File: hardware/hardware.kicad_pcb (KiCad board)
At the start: 2 copper layers, 1 part

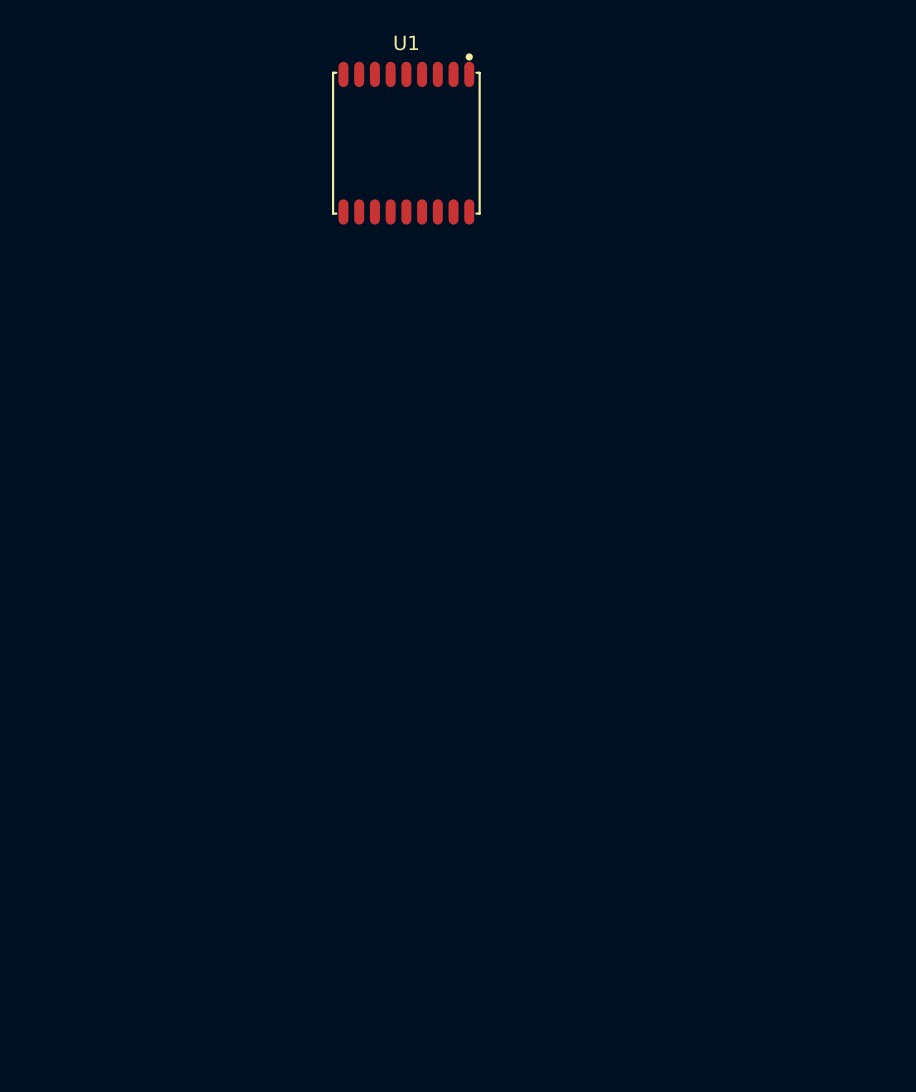
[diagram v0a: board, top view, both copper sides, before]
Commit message: place all components on pcb
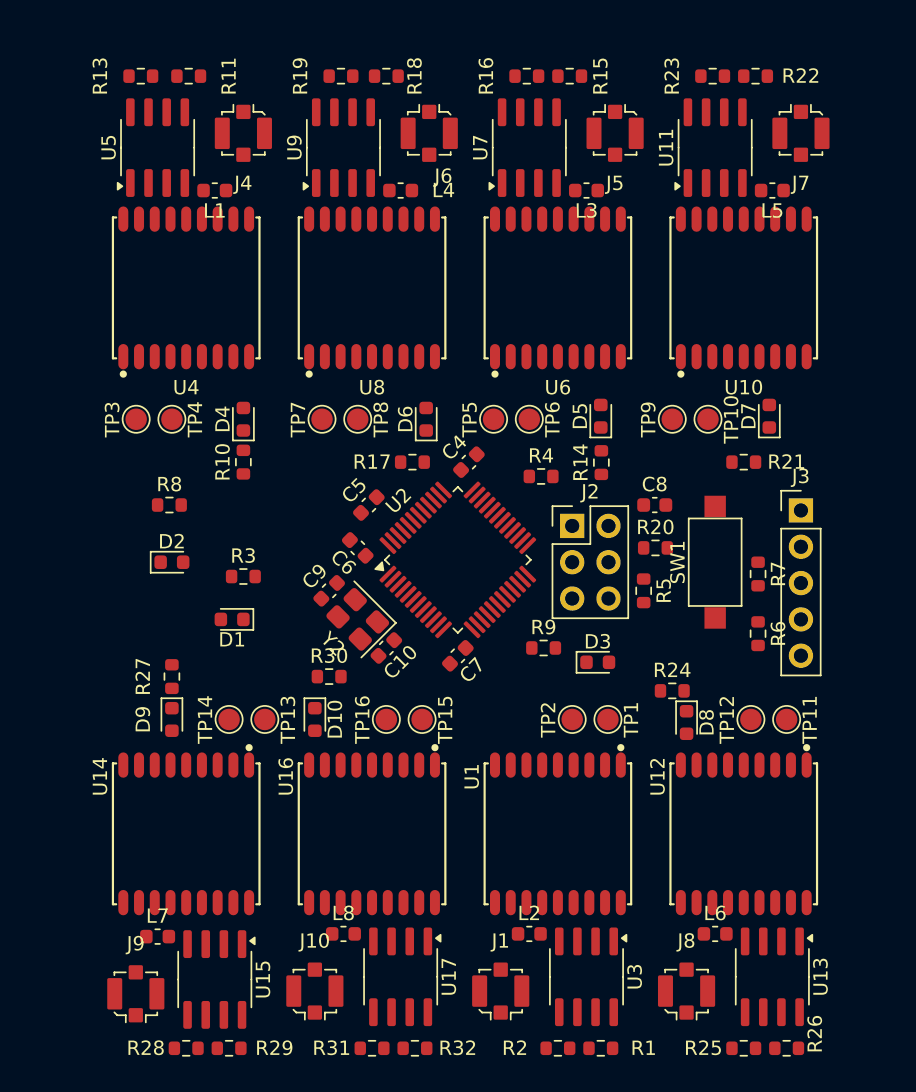
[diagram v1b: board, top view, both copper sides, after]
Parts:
- added C10: 20p, Capacitor_SMD:C_0603_1608Metric, F.Cu at (100.0, 107.0)
- added C4: 100n, Capacitor_SMD:C_0603_1608Metric, F.Cu at (105.8, 94.0)
- added C5: 100n, Capacitor_SMD:C_0603_1608Metric, F.Cu at (98.8, 97.0)
- added C6: 100n, Capacitor_SMD:C_0603_1608Metric, F.Cu at (98.0, 100.0)
- added C7: 100n, Capacitor_SMD:C_0603_1608Metric, F.Cu at (105.0, 107.5)
- added C8: 1u, Capacitor_SMD:C_0603_1608Metric, F.Cu at (118.8, 97.0)
- added C9: 20p, Capacitor_SMD:C_0603_1608Metric, F.Cu at (96.0, 103.0)
- added D1: LED, LED_SMD:LED_0603_1608Metric, F.Cu at (89.2, 105.0)
- added D10: LED, LED_SMD:LED_0603_1608Metric, F.Cu at (95.0, 112.0)
- added D2: LED, Diode_SMD:D_0603_1608Metric, F.Cu at (85.0, 101.0)
- added D3: LED, Diode_SMD:D_0603_1608Metric, F.Cu at (114.8, 108.0)
- added D4: LED, LED_SMD:LED_0603_1608Metric, F.Cu at (90.0, 91.0)
- added D5: LED, LED_SMD:LED_0603_1608Metric, F.Cu at (115.0, 90.8)
- added D6: LED, LED_SMD:LED_0603_1608Metric, F.Cu at (102.8, 91.0)
- added D7: LED, LED_SMD:LED_0603_1608Metric, F.Cu at (126.8, 90.8)
- added D8: LED, LED_SMD:LED_0603_1608Metric, F.Cu at (121.0, 112.2)
- added D9: LED, LED_SMD:LED_0603_1608Metric, F.Cu at (85.0, 112.0)
- added J1: Conn_Coaxial, Connector_Coaxial:U.FL_Molex_MCRF_73412-0110_Vertical, F.Cu at (108.0, 131.0)
- added J10: Conn_Coaxial, Connector_Coaxial:U.FL_Molex_MCRF_73412-0110_Vertical, F.Cu at (95.0, 131.0)
- added J2: BOOT, Connector_PinHeader_2.54mm:PinHeader_2x03_P2.54mm_Vertical, F.Cu at (113.0, 98.5)
- added J3: SWD, Connector_PinHeader_2.54mm:PinHeader_1x05_P2.54mm_Vertical, F.Cu at (129.0, 97.4)
- added J4: Conn_Coaxial, Connector_Coaxial:U.FL_Molex_MCRF_73412-0110_Vertical, F.Cu at (90.0, 71.0)
- added J5: Conn_Coaxial, Connector_Coaxial:U.FL_Molex_MCRF_73412-0110_Vertical, F.Cu at (116.0, 71.0)
- added J6: Conn_Coaxial, Connector_Coaxial:U.FL_Molex_MCRF_73412-0110_Vertical, F.Cu at (103.0, 71.0)
- added J7: Conn_Coaxial, Connector_Coaxial:U.FL_Molex_MCRF_73412-0110_Vertical, F.Cu at (129.0, 71.0)
- added J8: Conn_Coaxial, Connector_Coaxial:U.FL_Molex_MCRF_73412-0110_Vertical, F.Cu at (121.0, 131.0)
- added J9: Conn_Coaxial, Connector_Coaxial:U.FL_Molex_MCRF_73412-0110_Vertical, F.Cu at (82.5, 131.2)
- added L1: L_Small, Inductor_SMD:L_0603_1608Metric, F.Cu at (88.0, 75.0)
- added L2: L_Small, Inductor_SMD:L_0603_1608Metric, F.Cu at (110.0, 127.0)
- added L3: L_Small, Inductor_SMD:L_0603_1608Metric, F.Cu at (114.0, 75.0)
- added L4: L_Small, Inductor_SMD:L_0603_1608Metric, F.Cu at (101.0, 75.0)
- added L5: L_Small, Inductor_SMD:L_0603_1608Metric, F.Cu at (127.0, 75.0)
- added L6: L_Small, Inductor_SMD:L_0603_1608Metric, F.Cu at (123.0, 127.0)
- added L7: L_Small, Inductor_SMD:L_0603_1608Metric, F.Cu at (84.0, 127.2)
- added L8: L_Small, Inductor_SMD:L_0603_1608Metric, F.Cu at (97.0, 127.0)
- added R1: R_Small, Resistor_SMD:R_0603_1608Metric, F.Cu at (115.0, 135.0)
- added R10: 5K, Resistor_SMD:R_0603_1608Metric, F.Cu at (90.0, 94.0)
- added R11: R_Small, Resistor_SMD:R_0603_1608Metric, F.Cu at (86.2, 67.0)
- added R13: R_Small, Resistor_SMD:R_0603_1608Metric, F.Cu at (82.8, 67.0)
- added R14: 5K, Resistor_SMD:R_0603_1608Metric, F.Cu at (115.0, 94.0)
- added R15: R_Small, Resistor_SMD:R_0603_1608Metric, F.Cu at (112.8, 67.0)
- added R16: R_Small, Resistor_SMD:R_0603_1608Metric, F.Cu at (109.8, 67.0)
- added R17: 5K, Resistor_SMD:R_0603_1608Metric, F.Cu at (101.8, 94.0)
- added R18: R_Small, Resistor_SMD:R_0603_1608Metric, F.Cu at (100.0, 67.0)
- added R19: R_Small, Resistor_SMD:R_0603_1608Metric, F.Cu at (96.8, 67.0)
- added R2: R_Small, Resistor_SMD:R_0603_1608Metric, F.Cu at (112.0, 135.0)
- added R20: 10k, Resistor_SMD:R_0603_1608Metric, F.Cu at (118.8, 100.0)
- added R21: 5K, Resistor_SMD:R_0603_1608Metric, F.Cu at (125.0, 94.0)
- added R22: R_Small, Resistor_SMD:R_0603_1608Metric, F.Cu at (125.8, 67.0)
- added R23: R_Small, Resistor_SMD:R_0603_1608Metric, F.Cu at (122.8, 67.0)
- added R24: 5K, Resistor_SMD:R_0603_1608Metric, F.Cu at (120.0, 110.0)
- added R25: R_Small, Resistor_SMD:R_0603_1608Metric, F.Cu at (125.0, 135.0)
- added R26: R_Small, Resistor_SMD:R_0603_1608Metric, F.Cu at (128.0, 135.0)
- added R27: 5K, Resistor_SMD:R_0603_1608Metric, F.Cu at (85.0, 109.0)
- added R28: R_Small, Resistor_SMD:R_0603_1608Metric, F.Cu at (86.0, 135.0)
- added R29: R_Small, Resistor_SMD:R_0603_1608Metric, F.Cu at (89.0, 135.0)
- added R3: 5K, Resistor_SMD:R_0603_1608Metric, F.Cu at (90.0, 102.0)
- added R30: 5K, Resistor_SMD:R_0603_1608Metric, F.Cu at (96.0, 109.0)
- added R31: R_Small, Resistor_SMD:R_0603_1608Metric, F.Cu at (99.0, 135.0)
- added R32: R_Small, Resistor_SMD:R_0603_1608Metric, F.Cu at (102.0, 135.0)
- added R4: 100k, Resistor_SMD:R_0603_1608Metric, F.Cu at (110.8, 95.0)
- added R5: 100k, Resistor_SMD:R_0603_1608Metric, F.Cu at (118.0, 103.0)
- added R6: 10k, Resistor_SMD:R_0603_1608Metric, F.Cu at (126.0, 106.0)
- added R7: 10k, Resistor_SMD:R_0603_1608Metric, F.Cu at (126.0, 101.8)
- added R8: 10k, Resistor_SMD:R_0603_1608Metric, F.Cu at (84.8, 97.0)
- added R9: 10k, Resistor_SMD:R_0603_1608Metric, F.Cu at (111.0, 107.0)
- added SW1: SW_Push, Button_Switch_SMD:SW_SPST_CK_RS282G05A3, F.Cu at (123.0, 101.0)
- added TP1: TestPoint, TestPoint:TestPoint_Pad_D1.5mm, F.Cu at (115.5, 112.0)
- added TP10: TestPoint, TestPoint:TestPoint_Pad_D1.5mm, F.Cu at (122.5, 91.0)
- added TP11: TestPoint, TestPoint:TestPoint_Pad_D1.5mm, F.Cu at (128.0, 112.0)
- added TP12: TestPoint, TestPoint:TestPoint_Pad_D1.5mm, F.Cu at (125.5, 112.0)
- added TP13: TestPoint, TestPoint:TestPoint_Pad_D1.5mm, F.Cu at (91.5, 112.0)
- added TP14: TestPoint, TestPoint:TestPoint_Pad_D1.5mm, F.Cu at (89.0, 112.0)
- added TP15: TestPoint, TestPoint:TestPoint_Pad_D1.5mm, F.Cu at (102.5, 112.0)
- added TP16: TestPoint, TestPoint:TestPoint_Pad_D1.5mm, F.Cu at (100.0, 112.0)
- added TP2: TestPoint, TestPoint:TestPoint_Pad_D1.5mm, F.Cu at (113.0, 112.0)
- added TP3: TestPoint, TestPoint:TestPoint_Pad_D1.5mm, F.Cu at (82.5, 91.0)
- added TP4: TestPoint, TestPoint:TestPoint_Pad_D1.5mm, F.Cu at (85.0, 91.0)
- added TP5: TestPoint, TestPoint:TestPoint_Pad_D1.5mm, F.Cu at (107.5, 91.0)
- added TP6: TestPoint, TestPoint:TestPoint_Pad_D1.5mm, F.Cu at (110.0, 91.0)
- added TP7: TestPoint, TestPoint:TestPoint_Pad_D1.5mm, F.Cu at (95.5, 91.0)
- added TP8: TestPoint, TestPoint:TestPoint_Pad_D1.5mm, F.Cu at (98.0, 91.0)
- added TP9: TestPoint, TestPoint:TestPoint_Pad_D1.5mm, F.Cu at (120.0, 91.0)
- added U10: ~, ATGM336H:GPSM-SMD_ATGM336H-TR, F.Cu at (125.0, 81.8)
- added U11: 24LC32, Package_SO:SOIC-8_3.9x4.9mm_P1.27mm, F.Cu at (123.0, 72.0)
- added U12: ~, ATGM336H:GPSM-SMD_ATGM336H-TR, F.Cu at (125.0, 120.0)
- added U13: 24LC32, Package_SO:SOIC-8_3.9x4.9mm_P1.27mm, F.Cu at (127.0, 130.0)
- added U14: ~, ATGM336H:GPSM-SMD_ATGM336H-TR, F.Cu at (86.0, 120.0)
- added U15: 24LC32, Package_SO:SOIC-8_3.9x4.9mm_P1.27mm, F.Cu at (88.0, 130.2)
- added U16: ~, ATGM336H:GPSM-SMD_ATGM336H-TR, F.Cu at (99.0, 120.0)
- added U17: 24LC32, Package_SO:SOIC-8_3.9x4.9mm_P1.27mm, F.Cu at (101.0, 130.0)
- added U2: STM32F103C8Tx, Package_QFP:LQFP-48_7x7mm_P0.5mm, F.Cu at (105.0, 100.8)
- added U3: 24LC32, Package_SO:SOIC-8_3.9x4.9mm_P1.27mm, F.Cu at (114.0, 130.0)
- added U4: ~, ATGM336H:GPSM-SMD_ATGM336H-TR, F.Cu at (86.0, 81.8)
- added U5: 24LC32, Package_SO:SOIC-8_3.9x4.9mm_P1.27mm, F.Cu at (84.0, 72.0)
- added U6: ~, ATGM336H:GPSM-SMD_ATGM336H-TR, F.Cu at (112.0, 81.8)
- added U7: 24LC32, Package_SO:SOIC-8_3.9x4.9mm_P1.27mm, F.Cu at (110.0, 72.0)
- added U8: ~, ATGM336H:GPSM-SMD_ATGM336H-TR, F.Cu at (99.0, 81.8)
- added U9: 24LC32, Package_SO:SOIC-8_3.9x4.9mm_P1.27mm, F.Cu at (97.0, 72.0)
- added Y2: Crystal_GND24, Crystal:Crystal_SMD_3225-4Pin_3.2x2.5mm, F.Cu at (98.0, 105.0)
- moved U1 49.5 mm to (112.0, 120.0)
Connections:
- U1 pad 10: unconnected-(U1-GND-Pad10) -> GND
- U1 pad 11: unconnected-(U1-RF_IN-Pad11) -> Net-(J1-In)
- U1 pad 12: unconnected-(U1-GND-Pad12) -> GND
- U1 pad 14: unconnected-(U1-VCC_RF-Pad14) -> Net-(U1-VCC_RF)
- U1 pad 16: unconnected-(U1-SDA-Pad16) -> Net-(U1-SDA)
- U1 pad 17: unconnected-(U1-SCL-Pad17) -> Net-(U1-SCL)
- U1 pad 2: unconnected-(U1-TXD-Pad2) -> RX_1
- U1 pad 3: unconnected-(U1-RXD-Pad3) -> TX_1
- U1 pad 4: unconnected-(U1-1PPS-Pad4) -> Net-(D1-A)
- U1 pad 8: unconnected-(U1-VCC-Pad8) -> +3.3V
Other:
- copper layers 2 -> 4

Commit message: add power and comm connector
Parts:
- added J11: Conn_01x06_Pin, Connector_JST:JST_SH_BM06B-SRSS-TB_1x06-1MP_P1.00mm_Vertical, F.Cu at (82.0, 100.5)
- moved D2 9.69 mm to (94.2, 98.0)
- moved R8 5.44 mm to (90.2, 98.0)

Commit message: full wiring pcb
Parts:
- removed R4, R5: 100k, Resistor_SMD:R_0603_1608Metric
- moved D3 37.3 mm to (77.5, 107.5)
- moved R9 30.5 mm to (80.5, 107.5), turned to 180 degrees
- moved D1 22.0 mm to (110.0, 112.2), turned to -90 degrees
- moved R3 21.2 mm to (110.0, 109.2), turned to -90 degrees
- moved D2 17.1 mm to (77.3, 95.5)
- moved R8 10.2 mm to (80.3, 95.5), turned to 180 degrees
- moved J11 4.12 mm to (78.0, 101.5)
- moved D4 1.54 mm to (91.0, 89.8)
- moved R10 1.54 mm to (91.0, 92.8)
- moved TP3 1.50 mm to (84.0, 91.0)
- moved TP4 1.50 mm to (86.5, 91.0)
- moved R20 1.45 mm to (120.1, 100.7), turned to 90 degrees
- moved C8 1.45 mm to (120.1, 97.6), turned to 90 degrees
- moved D8 1.02 mm to (120.0, 112.0)
- moved D6 1.00 mm to (102.8, 90.0)
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- renumbered SW1 to RST
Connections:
- J2 pad 3: Net-(J2-Pin_3) -> BOOT0
- J2 pad 4: Net-(J2-Pin_4) -> BOOT1
- U2 pad 29: unconnected-(U2-PA8-Pad29) -> LED2
- U2 pad 30: unconnected-(U2-PA9-Pad30) -> LED1
- U2 pad 7: RST -> RESET
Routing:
- net GND: track 0.00 -> 236.4 mm, vias 0 -> 78
- net +3.3V: track 0.00 -> 106.1 mm, vias 0 -> 39
- net RESET: track 0.00 -> 41.6 mm, vias 0 -> 2
- net SWCLK: track 0.00 -> 41.1 mm, vias 0 -> 1
- net LED2: track 0.00 -> 37.9 mm, vias 0 -> 2
- net RX_2: track 0.00 -> 37.7 mm
- net TX_2: track 0.00 -> 34.6 mm
- net SWDIO: track 0.00 -> 32.8 mm, vias 0 -> 1
- net LED1: track 0.00 -> 31.7 mm, vias 0 -> 2
- net RX_6: track 0.00 -> 31.1 mm, vias 0 -> 2
- net SS: track 0.00 -> 29.5 mm, vias 0 -> 2
- net MOSI: track 0.00 -> 29.2 mm, vias 0 -> 2
- net MISO: track 0.00 -> 28.8 mm, vias 0 -> 2
- net TX_7: track 0.00 -> 27.9 mm
- net TX_6: track 0.00 -> 27.8 mm
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- added copper zone on F.Cu, net +3.3V
- added copper zone on In2.Cu, net +3.3V
- added copper zone on F.Cu, net GND
- added copper zone on In1.Cu, net GND
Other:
- board outline added: 60 x 71 mm

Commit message: add connector step
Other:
- outline, holes or cut-outs redrawn
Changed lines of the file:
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@@
 		)
 		(embedded_fonts no)
-		(model "${KICAD9_3DMODEL_DIR}/Connector_JST.3dshapes/JST_SH_BM06B-SRSS-TB_1x06-1MP_P1.00mm_Vertical.step"
+		(model "/Users/ronanmingon/Downloads/jst-sh-smd-connectors-1.snapshot.4/SMxxB-SRSS-TB/SM06B-SRSS-TB.STEP"
 			(offset
-				(xyz 0 0 0)
+				(xyz 0 -1 -0.4)
 			)
 			(scale
@@
 			)
 			(rotate
-				(xyz 0 0 0)
+				(xyz -90 -0 -180)
 			)
 		)
@@
 		)
 	)
+	(gr_circle
+		(center 132 91)
+		(end 133.6 91)
+		(stroke
+			(width 0.1)
+			(type solid)
+		)
+		(fill no)
+		(layer "Edge.Cuts")
+	)
 	(gr_line
 		(start 132 65)
@@
 		(layer "Edge.Cuts")
 	)
+	(gr_circle
+		(center 132 112)
+		(end 133.6 112)
+		(stroke
+			(width 0.1)
+			(type solid)
+		)
+		(fill no)
+		(layer "Edge.Cuts")
+	)
+	(gr_circle
+		(center 78 91)
+		(end 79.6 91)
+		(stroke
+			(width 0.1)
+			(type solid)
+		)
+		(fill no)
+		(layer "Edge.Cuts")
+	)
+	(gr_circle
+		(center 78 112)
+		(end 79.6 112)
+		(stroke
+			(width 0.1)
+			(type solid)
+		)
+		(fill no)
+		(layer "Edge.Cuts")
+	)

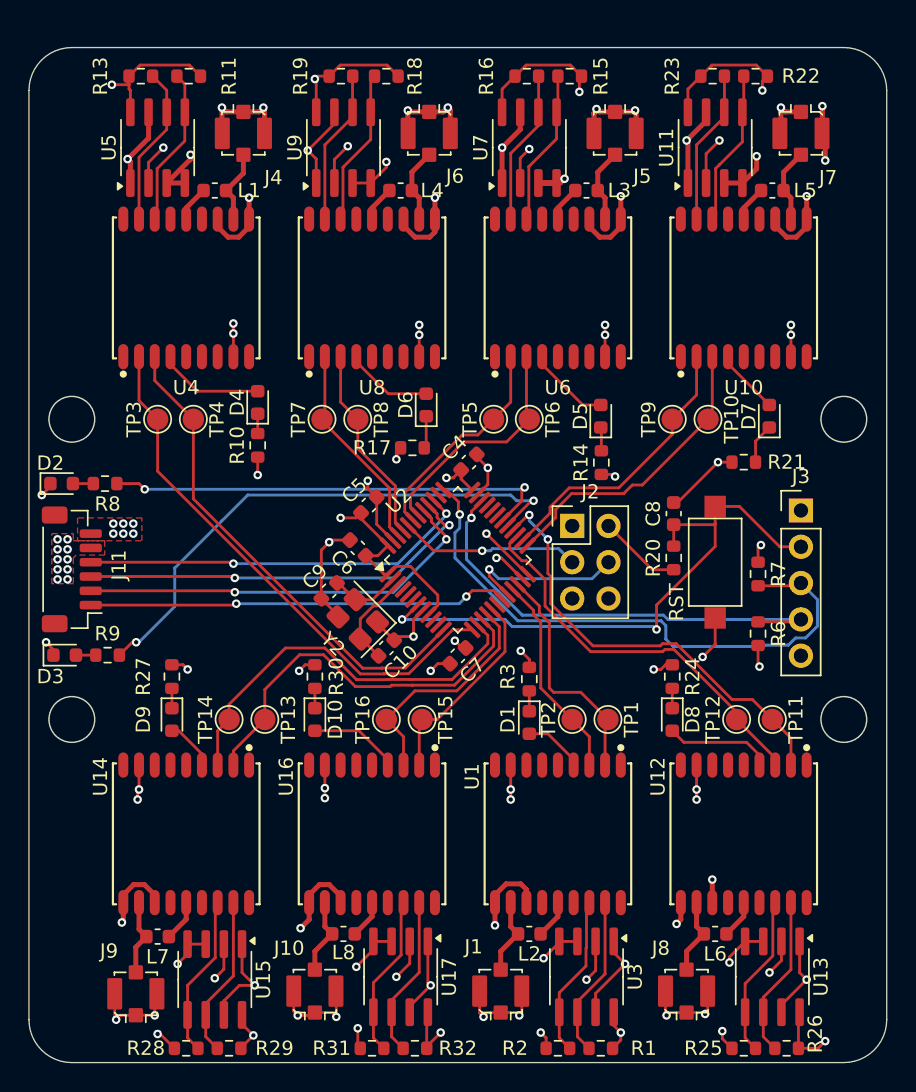
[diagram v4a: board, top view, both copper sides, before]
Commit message: fix gnss ground module
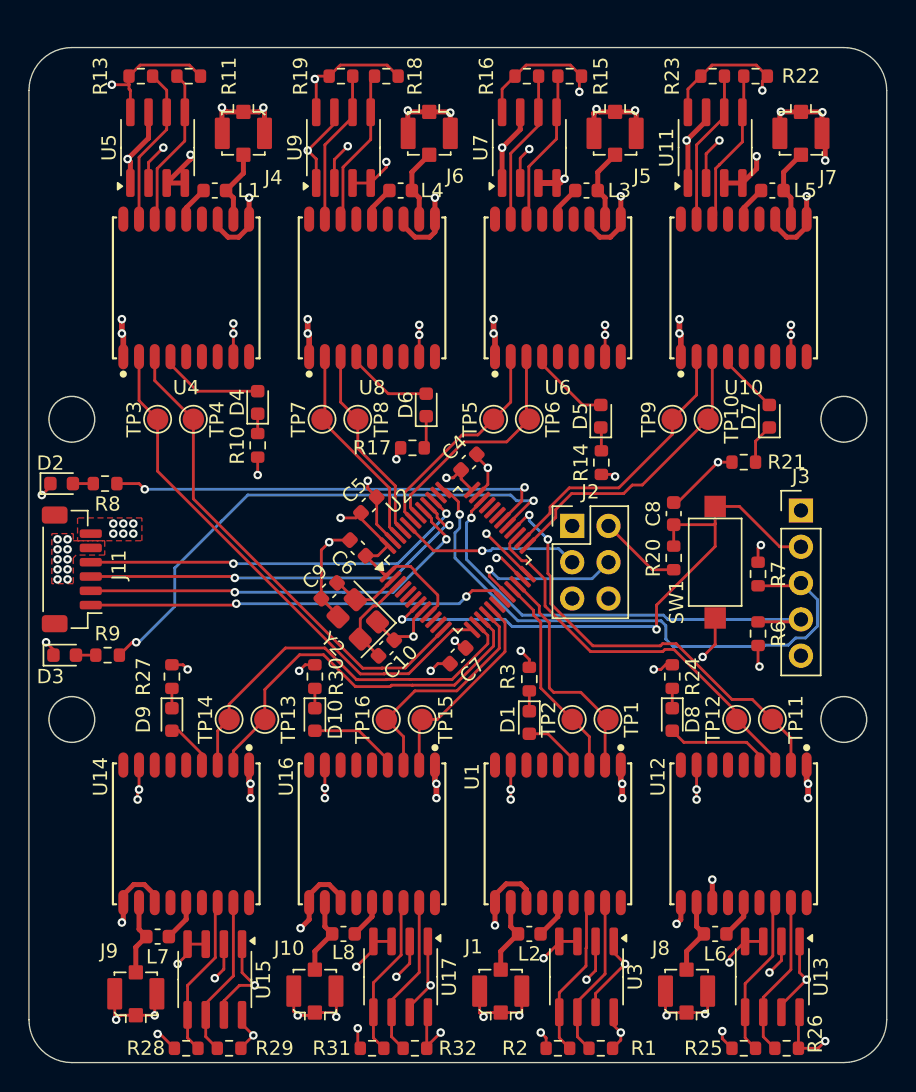
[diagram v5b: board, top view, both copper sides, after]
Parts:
- renumbered RST to SW1
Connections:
- U1 pad 1: unconnected-(U1-GND-Pad1) -> GND
- U10 pad 1: unconnected-(U10-GND-Pad1) -> GND
- U12 pad 1: unconnected-(U12-GND-Pad1) -> GND
- U14 pad 1: unconnected-(U14-GND-Pad1) -> GND
- U16 pad 1: unconnected-(U16-GND-Pad1) -> GND
- U4 pad 1: unconnected-(U4-GND-Pad1) -> GND
- U6 pad 1: unconnected-(U6-GND-Pad1) -> GND
- U8 pad 1: unconnected-(U8-GND-Pad1) -> GND
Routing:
- net GND: track 236.4 -> 256.8 mm, vias 78 -> 94
